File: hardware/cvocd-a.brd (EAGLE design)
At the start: 152.5 x 43.6 mm, 78 parts, among them IC1 6N138, IC2 LM324D, IC3 MCP4728_QUAD_DAC, IC4 REG1117, IC5 PIC16F1825SO14, IC6 74HC595D, IC7 74HC595D

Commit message: v5 pcb release candidate
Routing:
- net N$19: track 19.9 -> 20.7 mm
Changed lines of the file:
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@@
 <wire x1="49.723" y1="35.56" x2="49.53" y2="35.367" width="0.3048" layer="1"/>
 <wire x1="41.402" y1="33.467" x2="41.402" y2="33.147" width="0.3048" layer="1"/>
-<wire x1="41.402" y1="33.147" x2="45.212" y2="33.147" width="0.3048" layer="1"/>
+<wire x1="41.402" y1="33.147" x2="43.815" y2="33.147" width="0.3048" layer="1"/>
 <wire x1="45.212" y1="33.147" x2="45.466" y2="33.401" width="0.3048" layer="1"/>
 <wire x1="45.466" y1="33.401" x2="45.466" y2="34.29" width="0.3048" layer="1"/>
-<wire x1="45.212" y1="33.147" x2="43.815" y2="33.467" width="0" layer="19" extent="1-1"/>
+<wire x1="45.212" y1="33.147" x2="43.815" y2="33.147" width="0.3048" layer="1"/>
+<wire x1="43.815" y1="33.147" x2="43.815" y2="33.467" width="0.3048" layer="1"/>
 </signal>
 <signal name="VOUTA">
@@
 <wire x1="46.736" y1="25.4" x2="49.47" y2="25.4" width="0.3048" layer="1"/>
 <wire x1="49.47" y1="25.4" x2="49.53" y2="25.34" width="0.3048" layer="1"/>
-<wire x1="43.815" y1="35.052" x2="43.815" y2="35.367" width="0" layer="19" extent="1-16"/>
+<wire x1="43.815" y1="35.367" x2="43.18" y2="35.367" width="0.3048" layer="1"/>
+<wire x1="43.18" y1="35.367" x2="43.18" y2="35.56" width="0.3048" layer="1"/>
 </signal>
 <signal name="N$38">

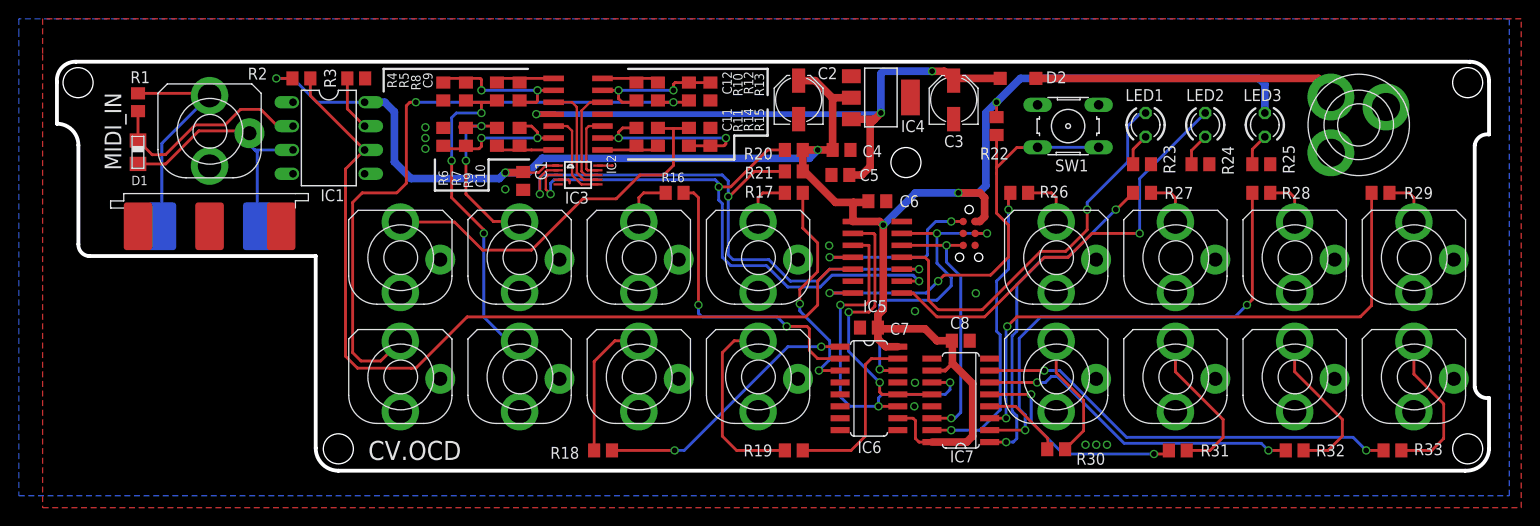
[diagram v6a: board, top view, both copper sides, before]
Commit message: V5.1 SILK SCREEN UPDATES
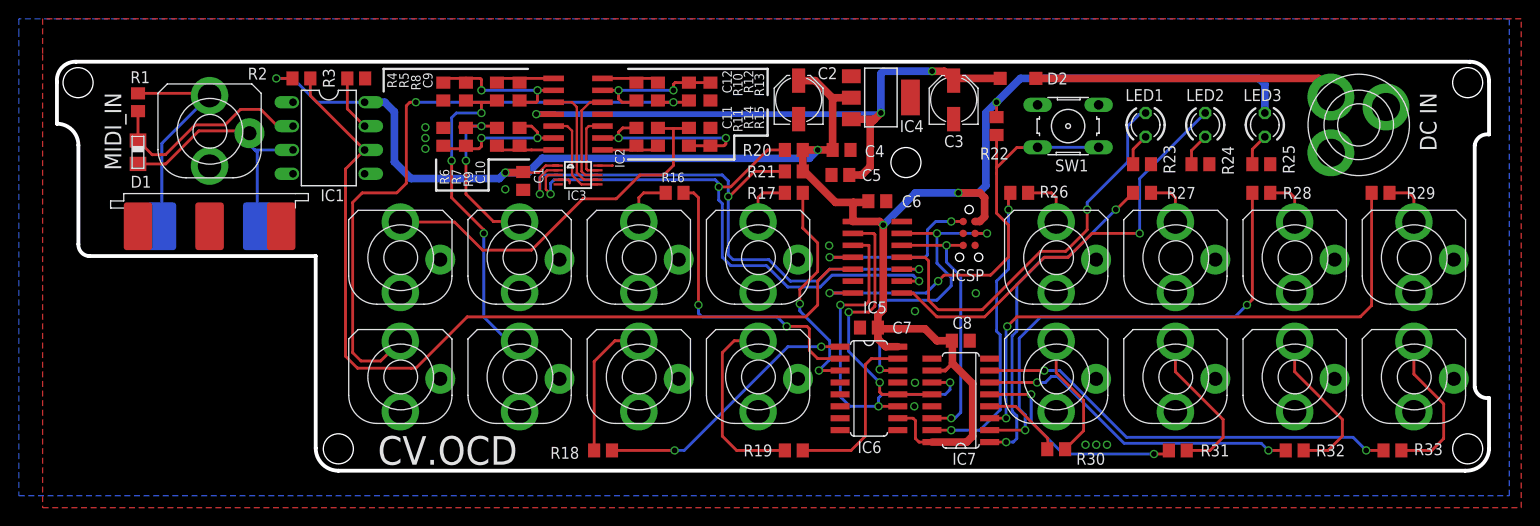
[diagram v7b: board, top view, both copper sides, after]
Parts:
- C10, C11, C12, C9: value 22p -> 20p
- C2, C3: value (none) -> 4u7
- C5, C6, C7, C8: value (none) -> 100n
- D2: value (none) -> 1N5819
- R1: value (none) -> 220
- R10, R11, R8, R9: value 220r -> 1k
- R12, R13, R14, R15, R4, R5, R6, R7: value 100k -> 10k/0.1%
- R16, R17, R18, R19, R23, R24, R25, R26, R27, R28, R29, R30, R31, R32, R33: value (none) -> 1k
- R22: value 10k -> 4k7
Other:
- board text added: "DC IN"

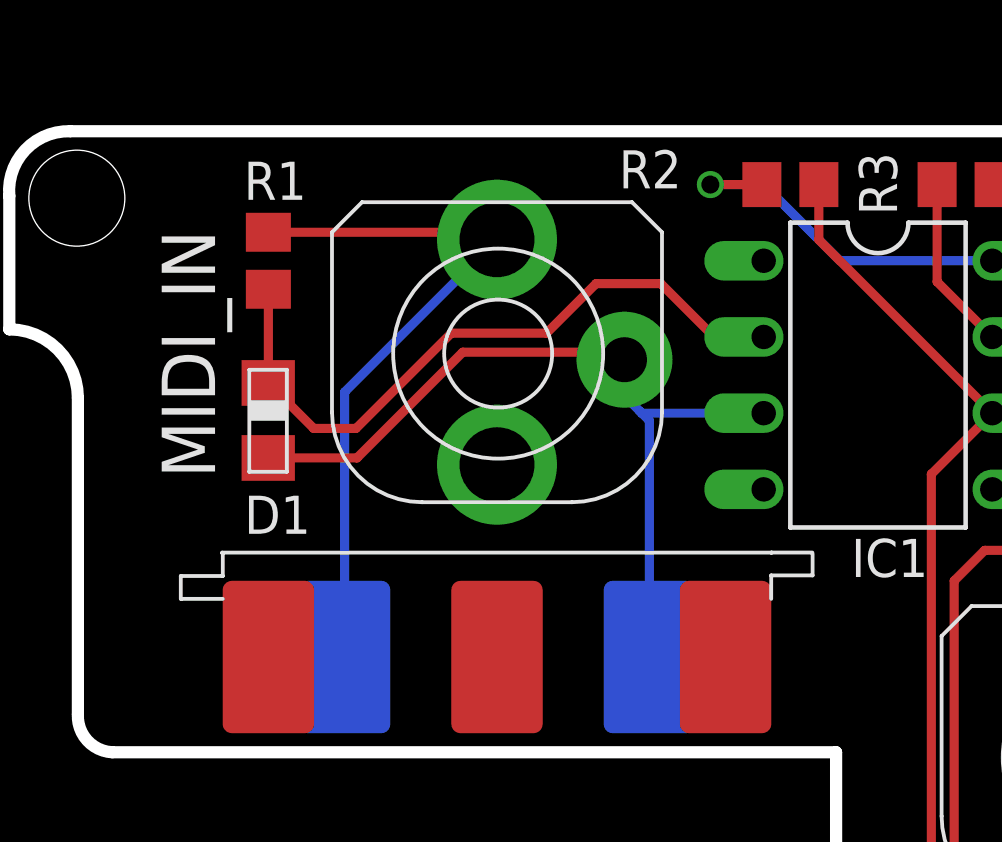
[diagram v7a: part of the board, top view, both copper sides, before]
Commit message: V6 candidate
change polarity on mini midi in socket
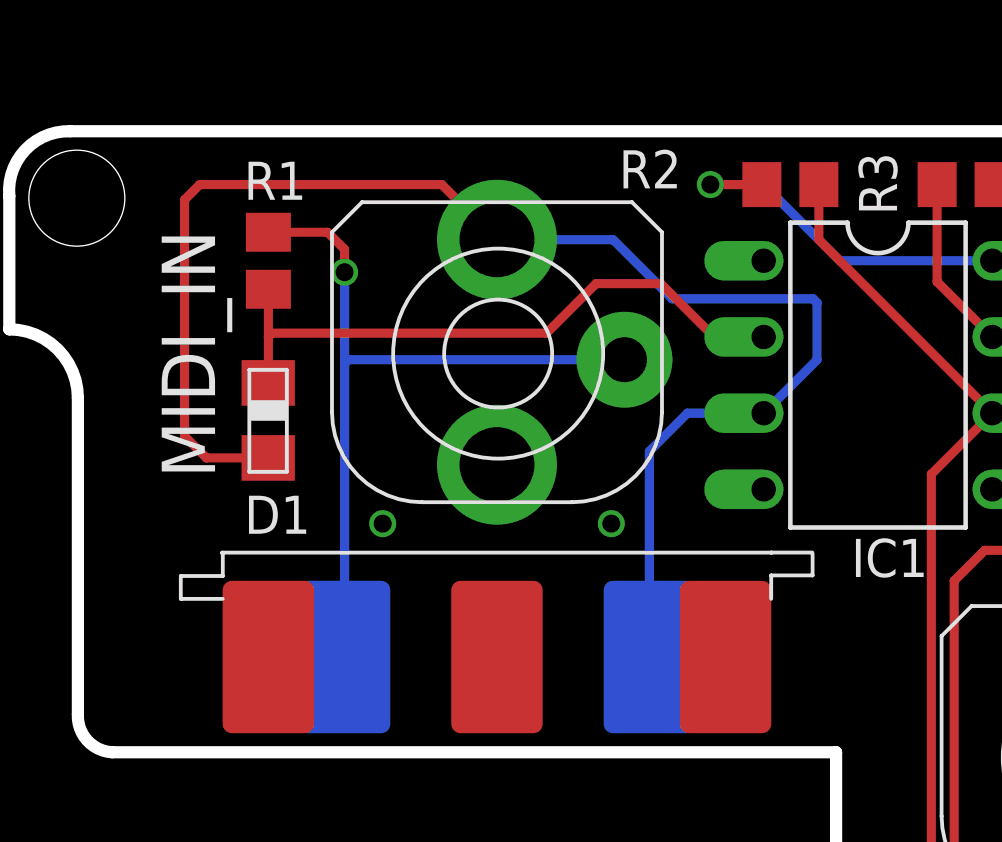
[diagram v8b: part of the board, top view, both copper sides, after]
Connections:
- net N$29: now also MIDI.3; no longer MIDI.4
- net N$31: now also MIDI.4; no longer MIDI.3
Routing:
- net N$31: track 27.8 -> 49.5 mm
- net N$29: track 23.7 -> 25.7 mm, vias 0 -> 1
- net N$30: track 23.0 -> 21.1 mm
- net GND: vias 12 -> 14
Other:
- board text added: "V6"
- board text removed: "V5"
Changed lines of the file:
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@@
 <wire x1="2.54" y1="33.528" x2="2.54" y2="22.987" width="0.4064" layer="20"/>
 <wire x1="2.54" y1="22.987" x2="3.683" y2="21.717" width="0.4064" layer="20" curve="90"/>
-<text x="28.702" y="10.414" size="2.54" layer="26" font="vector" ratio="20" rot="MR180">V5</text>
+<text x="28.702" y="10.414" size="2.54" layer="26" font="vector" ratio="20" rot="MR180">V6</text>
 <text x="5.207" y="23.241" size="2.032" layer="26" font="vector" ratio="20" rot="MR90">hotchk155</text>
 <hole x="90.678" y="31.678" drill="3.2"/>
@@
 <via x="39.497" y="34.29" extent="1-16" drill="0.6"/>
 <via x="39.497" y="33.147" extent="1-16" drill="0.6"/>
+<via x="12.7" y="29.337" extent="1-16" drill="0.6"/>
+<via x="20.32" y="29.337" extent="1-16" drill="0.6"/>
 </signal>
 <signal name="N$1">
@@
 <contactref element="MIDI_IN" pad="4"/>
 <contactref element="R1" pad="1"/>
-<contactref element="MIDI" pad="4"/>
-<wire x1="11.43" y1="24.892" x2="11.43" y2="33.722" width="0.3048" layer="16"/>
-<wire x1="11.43" y1="33.722" x2="16.51" y2="38.802" width="0.3048" layer="16"/>
-<wire x1="8.89" y1="39.05" x2="16.262" y2="39.05" width="0.3048" layer="1"/>
-<wire x1="16.262" y1="39.05" x2="16.51" y2="38.802" width="0.3048" layer="1"/>
+<wire x1="11.43" y1="24.892" x2="11.43" y2="34.671" width="0.3048" layer="16"/>
+<contactref element="MIDI" pad="3"/>
+<wire x1="11.43" y1="34.671" x2="11.43" y2="37.719" width="0.3048" layer="16"/>
+<wire x1="20.76" y1="34.802" x2="11.561" y2="34.802" width="0.3048" layer="16"/>
+<via x="11.43" y="37.719" extent="1-16" drill="0.6"/>
+<wire x1="11.43" y1="37.719" x2="11.43" y2="38.481" width="0.3048" layer="1"/>
+<wire x1="8.89" y1="39.05" x2="10.861" y2="39.05" width="0.3048" layer="1"/>
+<wire x1="10.861" y1="39.05" x2="11.43" y2="38.481" width="0.3048" layer="1"/>
+<wire x1="11.561" y1="34.802" x2="11.43" y2="34.671" width="0.3048" layer="16"/>
 </signal>
 <signal name="N$30">
@@
 <contactref element="IC1" pad="2"/>
 <contactref element="D1" pad="A"/>
-<wire x1="8.89" y1="37.15" x2="8.89" y2="34.0328" width="0.3048" layer="1"/>
+<wire x1="8.89" y1="37.15" x2="8.89" y2="35.56" width="0.3048" layer="1"/>
+<wire x1="8.89" y1="35.56" x2="8.89" y2="34.0328" width="0.3048" layer="1"/>
 <wire x1="8.89" y1="34.0328" x2="8.885" y2="34.0278" width="0.3048" layer="1"/>
 <wire x1="25.4" y1="35.56" x2="23.749" y2="35.56" width="0.3048" layer="1"/>
@@
 <wire x1="21.971" y1="37.338" x2="19.812" y2="37.338" width="0.3048" layer="1"/>
 <wire x1="19.812" y1="37.338" x2="18.161" y2="35.687" width="0.3048" layer="1"/>
-<wire x1="18.161" y1="35.687" x2="14.986" y2="35.687" width="0.3048" layer="1"/>
-<wire x1="14.986" y1="35.687" x2="11.811" y2="32.512" width="0.3048" layer="1"/>
-<wire x1="11.811" y1="32.512" x2="10.4008" y2="32.512" width="0.3048" layer="1"/>
-<wire x1="10.4008" y1="32.512" x2="8.885" y2="34.0278" width="0.3048" layer="1"/>
+<wire x1="18.161" y1="35.687" x2="9.017" y2="35.687" width="0.3048" layer="1"/>
+<wire x1="9.017" y1="35.687" x2="8.89" y2="35.56" width="0.3048" layer="1"/>
 </signal>
 <signal name="N$31">
@@
 <contactref element="MIDI_IN" pad="5"/>
 <contactref element="D1" pad="C"/>
-<contactref element="MIDI" pad="3"/>
-<wire x1="20.76" y1="33.596" x2="20.76" y2="34.802" width="0.3048" layer="16"/>
-<wire x1="25.4" y1="33.02" x2="21.336" y2="33.02" width="0.3048" layer="16"/>
-<wire x1="21.336" y1="33.02" x2="21.2725" y2="33.0835" width="0.3048" layer="16"/>
-<wire x1="21.2725" y1="33.0835" x2="20.76" y2="33.596" width="0.3048" layer="16"/>
-<wire x1="21.59" y1="24.892" x2="21.59" y2="32.766" width="0.3048" layer="16"/>
-<wire x1="21.59" y1="32.766" x2="21.336" y2="33.02" width="0.3048" layer="16"/>
-<wire x1="8.885" y1="31.5278" x2="11.8428" y2="31.5278" width="0.3048" layer="1"/>
-<wire x1="11.8428" y1="31.5278" x2="15.367" y2="35.052" width="0.3048" layer="1"/>
-<wire x1="15.367" y1="35.052" x2="20.51" y2="35.052" width="0.3048" layer="1"/>
-<wire x1="20.51" y1="35.052" x2="20.76" y2="34.802" width="0.3048" layer="1"/>
+<wire x1="21.59" y1="24.892" x2="21.59" y2="31.75" width="0.3048" layer="16"/>
+<contactref element="MIDI" pad="4"/>
+<wire x1="21.59" y1="31.75" x2="22.86" y2="33.02" width="0.3048" layer="16"/>
+<wire x1="22.86" y1="33.02" x2="25.4" y2="33.02" width="0.3048" layer="16"/>
+<wire x1="8.885" y1="31.5278" x2="6.8262" y2="31.5278" width="0.3048" layer="1"/>
+<wire x1="6.8262" y1="31.5278" x2="6.096" y2="32.258" width="0.3048" layer="1"/>
+<wire x1="6.096" y1="32.258" x2="6.096" y2="40.132" width="0.3048" layer="1"/>
+<wire x1="6.096" y1="40.132" x2="6.604" y2="40.64" width="0.3048" layer="1"/>
+<wire x1="6.604" y1="40.64" x2="14.672" y2="40.64" width="0.3048" layer="1"/>
+<wire x1="14.672" y1="40.64" x2="16.51" y2="38.802" width="0.3048" layer="1"/>
+<wire x1="16.51" y1="38.802" x2="20.38" y2="38.802" width="0.3048" layer="16"/>
+<wire x1="20.38" y1="38.802" x2="22.352" y2="36.83" width="0.3048" layer="16"/>
+<wire x1="22.352" y1="36.83" x2="27.051" y2="36.83" width="0.3048" layer="16"/>
+<wire x1="27.051" y1="36.83" x2="27.178" y2="36.703" width="0.3048" layer="16"/>
+<wire x1="27.178" y1="36.703" x2="27.178" y2="34.798" width="0.3048" layer="16"/>
+<wire x1="27.178" y1="34.798" x2="25.4" y2="33.02" width="0.3048" layer="16"/>
 </signal>
 <signal name="N$42">
